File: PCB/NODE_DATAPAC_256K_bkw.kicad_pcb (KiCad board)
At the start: 2 copper layers, 255.3 x 43.2 mm, 31 parts, among them J1 Conn_02x20_Odd_Even, U1 74161, U10 62256, U2 74161, U3 74161, U4 74138, U5 74138, U6 74374, U7 62256, U8 62256, U9 62256

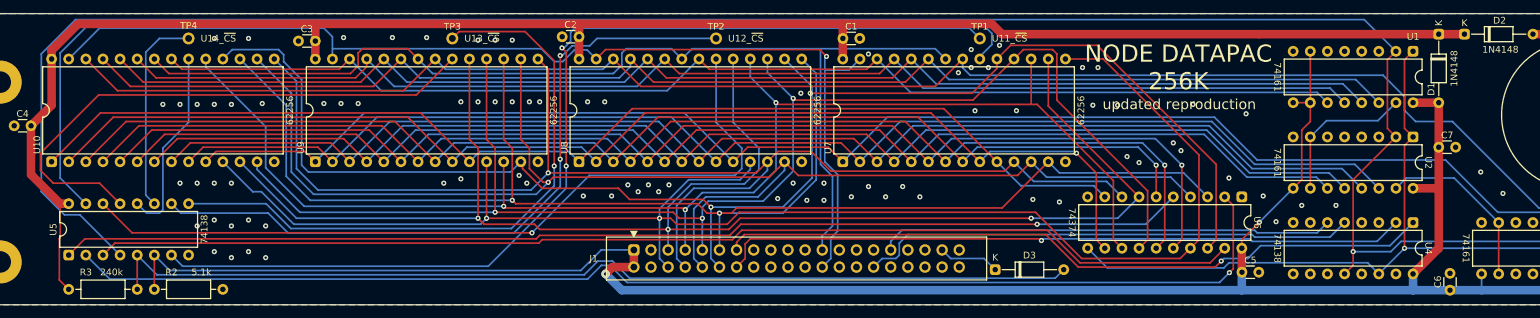
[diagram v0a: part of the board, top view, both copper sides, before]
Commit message: convert wires to busses in bkw sch
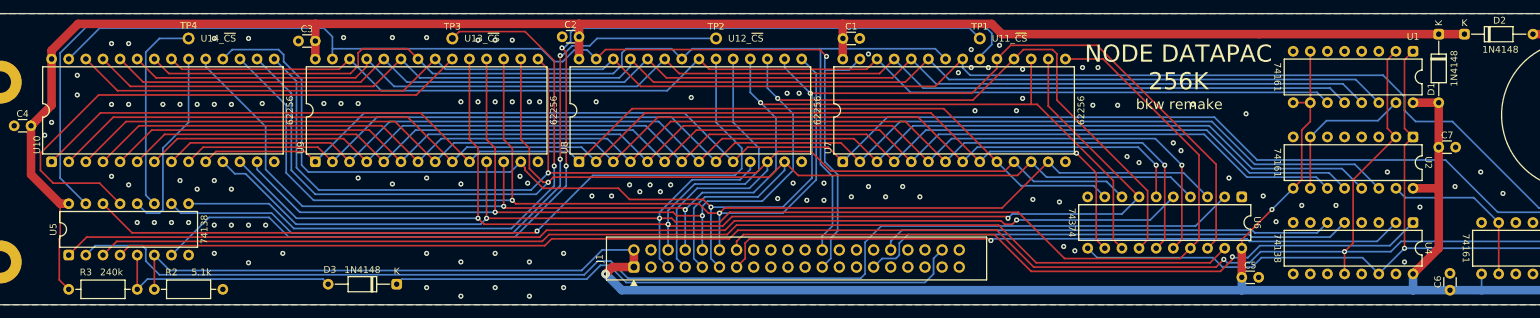
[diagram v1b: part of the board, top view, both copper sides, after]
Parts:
- J1: footprint 000_LOCAL:IDC_to_board_2x20_flipped -> 000_LOCAL:IDC_to_board_2x20
- moved D3 88.8 mm to (81.7, 116.3), turned to 180 degrees
- moved C5 0.76 mm to (207.0, 115.3)
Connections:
- net /TC0 renamed /CARRY0
- net /TC1 renamed /CARRY1
- net Net-(U1-CP) renamed /~{BYTE}
- net Net-(U1-~{MR}) renamed /~{BLOCK}
- J1 pad 10: /AD5 -> /AD4
- J1 pad 11: /AD6 -> /AD7
- J1 pad 12: /AD7 -> /AD6
- J1 pad 13: /BUS_A8 -> /BUS_A9
- J1 pad 14: /BUS_A9 -> /BUS_A8
- J1 pad 23: /~{RD} -> /~{WR}
- J1 pad 24: /~{WR} -> /~{RD}
- J1 pad 29: unconnected-(J1-Pin_29-Pad29) -> /Y0
- J1 pad 30: /Y0 -> unconnected-(J1-Pin_30-Pad30)
- J1 pad 31: /~{A} -> unconnected-(J1-Pin_31-Pad31)
- J1 pad 32: unconnected-(J1-Pin_32-Pad32) -> /~{A}
- J1 pad 37: /RAM_RST -> unconnected-(J1-Pin_37-Pad37)
- J1 pad 38: unconnected-(J1-Pin_38-Pad38) -> /RAM_RST
- J1 pad 5: /AD0 -> /AD1
- J1 pad 6: /AD1 -> /AD0
- J1 pad 7: /AD2 -> /AD3
- J1 pad 8: /AD3 -> /AD2
- J1 pad 9: /AD4 -> /AD5
- U1 pad 11: /A8 -> /A3
- U1 pad 12: /A7 -> /A2
- U1 pad 13: /A6 -> /A1
- U1 pad 14: /A5 -> /A0
- U10 pad 1: /A1 -> /A13
- U10 pad 10: /A14 -> /A9
- U10 pad 2: /A2 -> /A12
- U10 pad 21: /A8 -> /A3
- U10 pad 23: /A7 -> /A2
- U10 pad 24: /A6 -> /A1
- U10 pad 25: /A5 -> /A0
- U10 pad 26: /A13 -> /A8
- U10 pad 3: /A0 -> /A10
- U10 pad 4: /A3 -> /A14
- U10 pad 5: /A4 -> /A11
- U10 pad 6: /A12 -> /A7
- U10 pad 7: /A11 -> /A6
- U10 pad 8: /A10 -> /A5
- U10 pad 9: /A9 -> /A4
- U2 pad 11: /A12 -> /A7
- U2 pad 12: /A11 -> /A6
- U2 pad 13: /A10 -> /A5
- U2 pad 14: /A9 -> /A4
- U3 pad 13: /A14 -> /A9
- U3 pad 14: /A13 -> /A8
- U6 pad 12: /A2 -> /A12
- U6 pad 15: /A3 -> /A14
- U6 pad 16: /A4 -> /A11
- U6 pad 6: /A0 -> /A10
- U6 pad 9: /A1 -> /A13
- U7 pad 1: /A14 -> /A9
- U7 pad 10: /A1 -> /A13
- U7 pad 2: /A9 -> /A4
- U7 pad 21: /A13 -> /A8
- U7 pad 23: /A5 -> /A0
- U7 pad 24: /A6 -> /A1
- U7 pad 25: /A7 -> /A2
- U7 pad 26: /A8 -> /A3
- U7 pad 3: /A10 -> /A5
- U7 pad 4: /A11 -> /A6
- U7 pad 5: /A12 -> /A7
- U7 pad 6: /A4 -> /A11
- U7 pad 7: /A3 -> /A14
- U7 pad 8: /A0 -> /A10
- U7 pad 9: /A2 -> /A12
- U8 pad 1: /A1 -> /A13
- U8 pad 10: /A14 -> /A9
- U8 pad 2: /A2 -> /A12
- U8 pad 21: /A8 -> /A3
- U8 pad 23: /A7 -> /A2
- U8 pad 24: /A6 -> /A1
- U8 pad 25: /A5 -> /A0
- U8 pad 26: /A13 -> /A8
- U8 pad 3: /A0 -> /A10
- U8 pad 4: /A3 -> /A14
- U8 pad 5: /A4 -> /A11
- U8 pad 6: /A12 -> /A7
- U8 pad 7: /A11 -> /A6
- U8 pad 8: /A10 -> /A5
- U8 pad 9: /A9 -> /A4
- U9 pad 1: /A14 -> /A9
- U9 pad 10: /A1 -> /A13
- U9 pad 2: /A9 -> /A4
- U9 pad 21: /A13 -> /A8
- U9 pad 23: /A5 -> /A0
- U9 pad 24: /A6 -> /A1
- U9 pad 25: /A7 -> /A2
- U9 pad 26: /A8 -> /A3
- U9 pad 3: /A10 -> /A5
- U9 pad 4: /A11 -> /A6
- U9 pad 5: /A12 -> /A7
- U9 pad 6: /A4 -> /A11
- U9 pad 7: /A3 -> /A14
- U9 pad 8: /A0 -> /A10
- U9 pad 9: /A2 -> /A12
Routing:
- net /SLEEP: track 146.1 -> 34.3 mm
- net /A13: track 259.5 -> 172.1 mm
- net /A8: track 180.6 -> 259.5 mm
- net /RAM_RST: track 9.08 -> 86.4 mm
- net /A14: track 240.3 -> 185.1 mm, vias 0 -> 1
- net /~{BYTE}: track 314.3 -> 261.3 mm, vias 1 -> 2
- net /A9: track 192.7 -> 240.3 mm
- net /A0: track 178.2 -> 201.1 mm, vias 1 -> 0
- net /A1: track 172.1 -> 194.8 mm
- net /A10: track 192.7 -> 178.2 mm, vias 0 -> 1
- net /A12: track 192.7 -> 179.3 mm, vias 0 -> 1
- net /A2: track 179.3 -> 189.9 mm, vias 1 -> 0
- net /A5: track 201.1 -> 192.7 mm
- net /A4: track 185.1 -> 192.7 mm, vias 1 -> 0
- net /A11: track 192.7 -> 185.1 mm, vias 0 -> 1
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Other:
- board text added: "bkw remake"
- board text removed: "A10"
- board text removed: "A11"
- board text removed: "A12"
- board text removed: "A13"
- board text removed: "A14"
- board text removed: "A15"
- board text removed: "CLK"
- board text removed: "INTR"
- board text removed: "IO/~{M}"
- board text removed: "S0"
- board text removed: "S1"
- board text removed: "nc"
- board text removed: "updated reproduction"
- board text removed: "~{ALE}"
- board text removed: "~{RESET}"

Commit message: schematic notes
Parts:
- C1, C2, C3, C4, C5, C6, C7: value 0.1u -> 1u
- turned TP1 to 0 degrees
- turned TP2 to 0 degrees
- turned TP3 to 0 degrees
- turned TP4 to 0 degrees
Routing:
- net /A16: track 182.0 -> 179.8 mm
- net GND: vias 120 -> 127

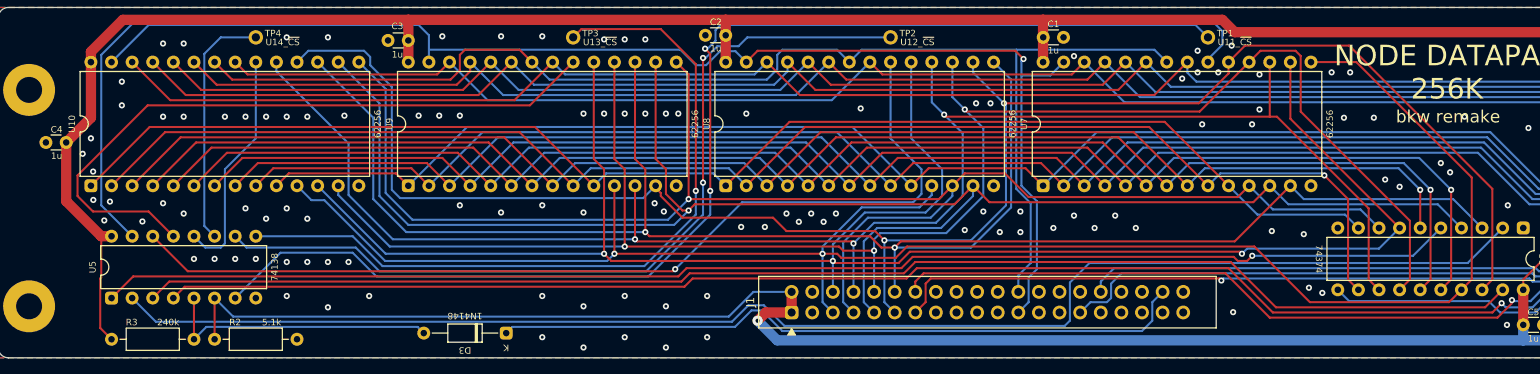
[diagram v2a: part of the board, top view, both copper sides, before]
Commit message: fix wrong polarity on net names (A), /Y0, /INTA, INTR, RESET
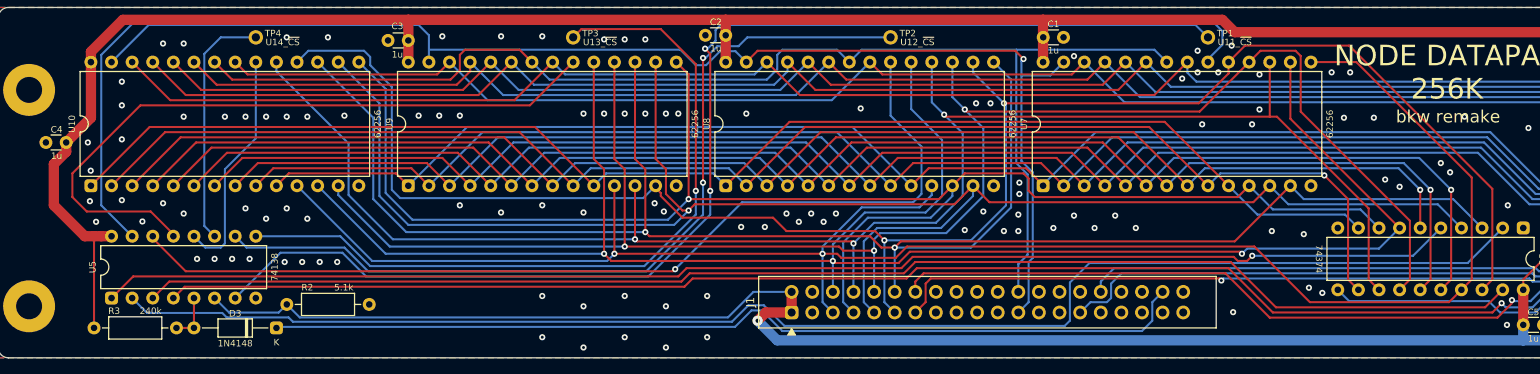
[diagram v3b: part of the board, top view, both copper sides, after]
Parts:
- moved D3 28.3 mm to (53.3, 115.7)
- moved R2 9.88 mm to (54.6, 112.8)
- moved R3 2.57 mm to (30.9, 115.7)
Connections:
- net /RAM_RST renamed /RAMRST
- net /Y0 renamed /~{Y0}
- net /~{A} renamed /(A)
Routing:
- net /SLEEP: track 34.3 -> 5.84 mm
- net /RAMRST: track 86.4 -> 114.5 mm
- net VBUS: track 317.5 -> 313.3 mm
- net /~{CS2}: track 83.3 -> 84.9 mm
- net /AD3: track 191.4 -> 192.3 mm
- net GND: vias 127 -> 125

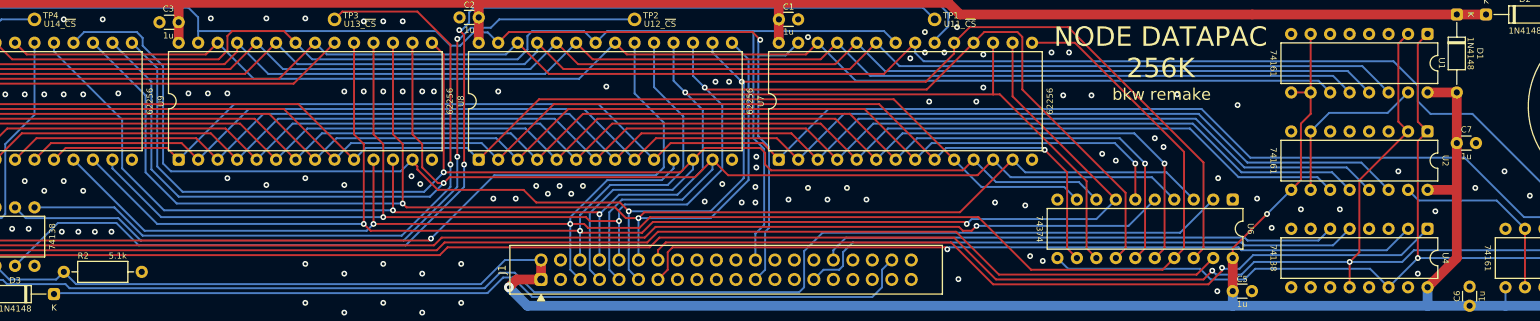
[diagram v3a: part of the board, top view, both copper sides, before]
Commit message: 512k support
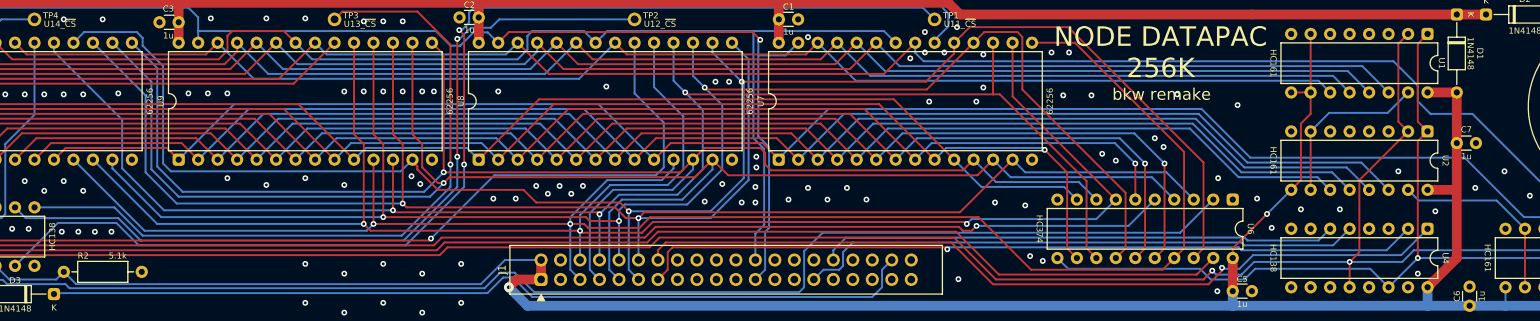
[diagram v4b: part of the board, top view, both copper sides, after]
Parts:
- U1, U2, U3: value 74161 -> HC161
- U4, U5: value 74138 -> HC138
- U6: value 74374 -> HC374
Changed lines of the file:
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@@
         (effects (font (size 0.8 0.8) (thickness 0.1)))
     )
-    (fp_text value "74161" (at 3.81 20.11 -90 unlocked) (layer "F.SilkS")
+    (fp_text value "HC161" (at 3.81 20.11 -90 unlocked) (layer "F.SilkS")
         (effects (font (size 0.8 0.8) (thickness 0.1)))
     )
@@
         (effects (font (size 0.8 0.8) (thickness 0.1)))
     )
-    (fp_text value "74161" (at 3.81 20.11 -90 unlocked) (layer "F.SilkS")
+    (fp_text value "HC161" (at 3.81 20.11 -90 unlocked) (layer "F.SilkS")
         (effects (font (size 0.8 0.8) (thickness 0.1)))
     )
@@
         (effects (font (size 0.8 0.8) (thickness 0.1)))
     )
-    (fp_text value "74138" (at 3.81 20.11 -90 unlocked) (layer "F.SilkS")
+    (fp_text value "HC138" (at 3.81 20.11 -90 unlocked) (layer "F.SilkS")
         (effects (font (size 0.8 0.8) (thickness 0.1)))
     )
@@
         (effects (font (size 0.8 0.8) (thickness 0.1)))
     )
-    (fp_text value "74374" (at 3.81 25.19 -90 unlocked) (layer "F.SilkS")
+    (fp_text value "HC374" (at 3.81 25.19 -90 unlocked) (layer "F.SilkS")
         (effects (font (size 0.8 0.8) (thickness 0.1)))
     )
@@
         (effects (font (size 0.8 0.8) (thickness 0.1)))
     )
-    (fp_text value "74161" (at 3.81 20.11 -90 unlocked) (layer "F.SilkS")
+    (fp_text value "HC161" (at 3.81 20.11 -90 unlocked) (layer "F.SilkS")
         (effects (font (size 0.8 0.8) (thickness 0.1)))
     )
@@
         (effects (font (size 0.8 0.8) (thickness 0.1)))
     )
-    (fp_text value "74138" (at 3.81 20.11 90 unlocked) (layer "F.SilkS")
-        (effects (font (size 0.8 0.8) (thickness 0.1)))
-    )
+    (fp_text value "HC138" (at 3.81 20.11 90 unlocked) (layer "F.SilkS")
+        (effects (font (size 0.8 0.8) (thickness 0.1)))
+    )
